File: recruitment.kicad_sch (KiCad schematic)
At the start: 12 parts, among them K1 Relay_SPST-NO, U1 OKI-78SR-5_1.5-W36-C

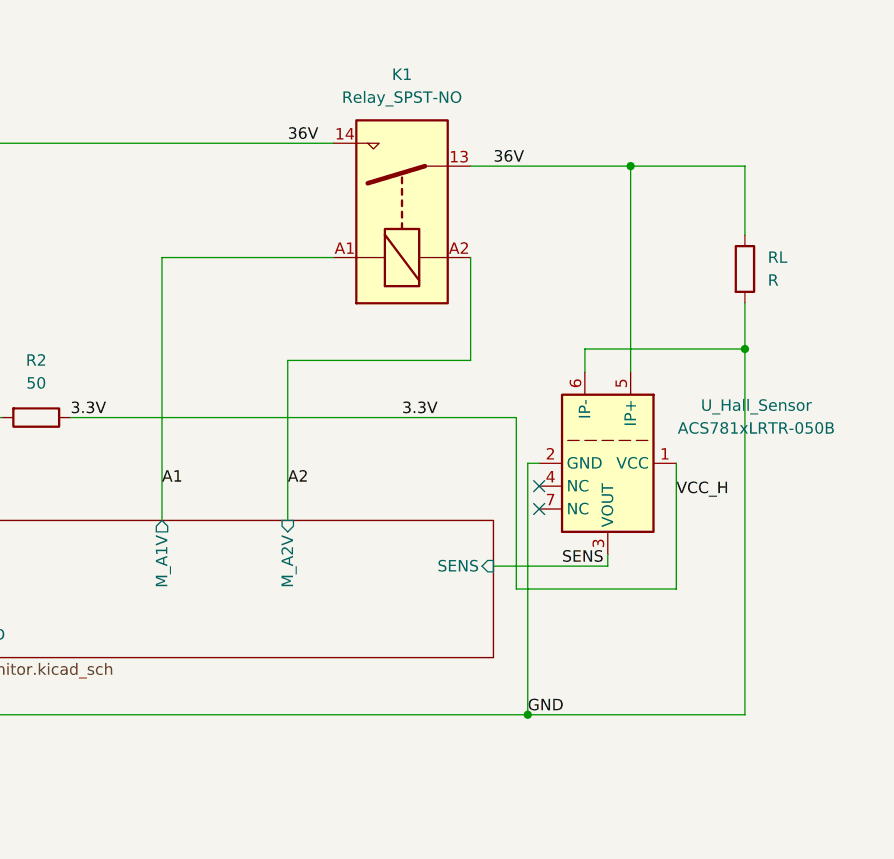
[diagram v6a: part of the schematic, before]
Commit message: comparator wirirng
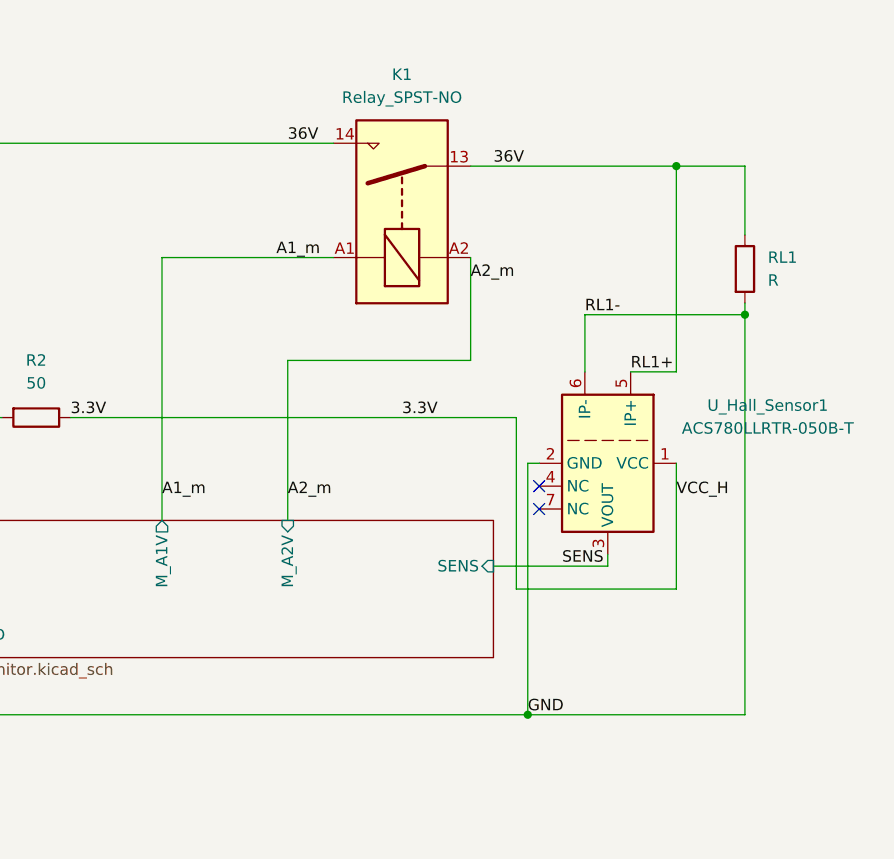
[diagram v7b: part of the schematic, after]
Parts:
- C1: footprint (none) -> Capacitor_SMD:C_0201_0603Metric
- K1: footprint (none) -> LED_THT:LED_D3.0mm
- R1, R2, R3, R4: footprint (none) -> Resistor_SMD:R_0201_0603Metric
- RL1: renamed from RL; footprint (none) -> Resistor_SMD:R_0201_0603Metric
- U_Hall_Sensor1: renamed from U_Hall_Sensor; value ACS781xLRTR-050B -> ACS780LLRTR-050B-T
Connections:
- net A1 renamed A1_m
- net A2 renamed A2_m
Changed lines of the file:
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@@
-	)
-	(junction
-		(at 196.85 41.91)
-		(diameter 0)
-		(color 0 0 0 0)
 	)
 	(junction
@@
 	)
 	(junction
-		(at 209.55 62.23)
-		(diameter 0)
-		(color 0 0 0 0)
-	)
-	(junction
 		(at 115.57 80.01)
 		(diameter 0)
@@
 	)
 	(junction
+		(at 209.55 58.42)
+		(diameter 0)
+		(color 0 0 0 0)
+	)
+	(junction
 		(at 54.61 102.87)
 		(diameter 0)
@@
 	)
 	(junction
+		(at 201.93 41.91)
+		(diameter 0)
+		(color 0 0 0 0)
+	)
+	(junction
 		(at 185.42 102.87)
 		(diameter 0)
@@
 	(wire
 		(pts
-			(xy 196.85 64.77) (xy 196.85 41.91)
-		)
-		(stroke
-			(width 0)
-			(type default)
-		)
-	)
-	(wire
-		(pts
-			(xy 209.55 57.15) (xy 209.55 62.23)
+			(xy 158.75 63.5) (xy 158.75 81.28)
+		)
+		(stroke
+			(width 0)
+			(type default)
+		)
+	)
+	(wire
+		(pts
+			(xy 201.93 64.77) (xy 201.93 41.91)
+		)
+		(stroke
+			(width 0)
+			(type default)
+		)
+	)
+	(wire
+		(pts
+			(xy 209.55 57.15) (xy 209.55 58.42)
 		)
 		(stroke
@@
 	(wire
 		(pts
-			(xy 191.77 62.23) (xy 191.77 64.77)
-		)
-		(stroke
-			(width 0)
-			(type default)
-		)
-	)
-	(wire
-		(pts
 			(xy 46.99 80.01) (xy 67.31 80.01)
 		)
@@
 	(wire
 		(pts
-			(xy 209.55 62.23) (xy 191.77 62.23)
+			(xy 209.55 58.42) (xy 191.77 58.42)
 		)
 		(stroke
@@
 	(wire
 		(pts
-			(xy 209.55 62.23) (xy 209.55 102.87)
+			(xy 209.55 58.42) (xy 209.55 102.87)
 		)
 		(stroke
@@
 	(wire
 		(pts
+			(xy 201.93 41.91) (xy 209.55 41.91)
+		)
+		(stroke
+			(width 0)
+			(type default)
+		)
+	)
+	(wire
+		(pts
 			(xy 74.93 87.63) (xy 74.93 102.87)
 		)
@@
 	(wire
 		(pts
-			(xy 179.07 41.91) (xy 196.85 41.91)
+			(xy 179.07 41.91) (xy 201.93 41.91)
 		)
 		(stroke
@@
 	(wire
 		(pts
-			(xy 158.75 81.28) (xy 158.75 63.5)
+			(xy 191.77 58.42) (xy 191.77 64.77)
 		)
 		(stroke
@@
 	(wire
 		(pts
+			(xy 201.93 64.77) (xy 196.85 64.77)
+		)
+		(stroke
+			(width 0)
+			(type default)
+		)
+	)
+	(wire
+		(pts
 			(xy 185.42 102.87) (xy 209.55 102.87)
 		)
@@
 	(wire
 		(pts
-			(xy 144.78 81.28) (xy 144.78 52.07)
+			(xy 144.78 52.07) (xy 144.78 81.28)
 		)
 		(stroke
@@
 		(pts
 			(xy 181.61 86.36) (xy 194.31 86.36)
-		)
-		(stroke
-			(width 0)
-			(type default)
-		)
-	)
-	(wire
-		(pts
-			(xy 196.85 41.91) (xy 209.55 41.91)
 		)
 		(stroke
@@
 		)
 	)
+	(label "RL1+"
+		(at 196.85 64.77 0)
+		(effects
+			(font
+				(size 1.27 1.27)
+			)
+			(justify left bottom)
+		)
+	)
 	(label "9-17V"
 		(at 60.96 80.01 0)
@@
 		)
 	)
+	(label "A1_m"
+		(at 157.48 52.07 0)
+		(effects
+			(font
+				(size 1.27 1.27)
+			)
+			(justify left bottom)
+		)
+	)
 	(label "3.3V"
 		(at 171.45 69.85 0)
@@
 		)
 	)
+	(label "RL1-"
+		(at 191.77 58.42 0)
+		(effects
+			(font
+				(size 1.27 1.27)
+			)
+			(justify left bottom)
+		)
+	)
 	(label "GND"
 		(at 185.42 102.87 0)
@@
 		)
 	)
-	(label "A1"
-		(at 144.78 77.47 0)
+	(label "A1_m"
+		(at 144.78 78.74 0)
 		(effects
 			(font
@@
 		)
 	)
-	(label "A2"
-		(at 158.75 77.47 0)
+	(label "A2_m"
+		(at 158.75 78.74 0)
+		(effects
+			(font
+				(size 1.27 1.27)
+			)
+			(justify left bottom)
+		)
+	)
+	(label "A2_m"
+		(at 179.07 54.61 0)
 		(effects
 			(font
@@
 		(dnp no)
 		(fields_autoplaced yes)
-		(property "Reference" "U_Hall_Sensor"
-			(at 210.82 68.5098 90)
-			(effects
-				(font
-					(size 1.27 1.27)
-				)
-			)
-		)
-		(property "Value" "ACS781xLRTR-050B"
-			(at 210.82 71.0498 90)
+		(property "Reference" "U_Hall_Sensor1"
+			(at 212.09 68.5098 90)
+			(effects
+				(font
+					(size 1.27 1.27)
+				)
+			)
+		)
+		(property "Value" "ACS780LLRTR-050B-T"
+			(at 212.09 71.0498 90)
 			(effects
 				(font
@@
 			(project ""
 				(path "/bdc7face-9f7c-4701-80bb-4cc144448db1"
-					(reference "U_Hall_Sensor")
+					(reference "U_Hall_Sensor1")
 					(unit 1)
 				)
@@
 			)
 		)
-		(property "Footprint" ""
+		(property "Footprint" "Resistor_SMD:R_0201_0603Metric"
 			(at 119.888 43.18 90)
 			(effects
@@
 			)
 		)
-		(property "Footprint" ""
+		(property "Footprint" "Capacitor_SMD:C_0201_0603Metric"
 			(at 47.9552 97.79 0)
 			(effects
@@
 			)
 		)
-		(property "Footprint" ""
+		(property "Footprint" "Resistor_SMD:R_0201_0603Metric"
 			(at 91.948 87.63 90)
 			(effects
@@
 		(dnp no)
 		(fields_autoplaced yes)
-		(property "Reference" "RL"
+		(property "Reference" "RL1"
 			(at 212.09 52.0699 0)
 			(effects
@@
 			)
 		)
-		(property "Footprint" ""
+		(property "Footprint" "Resistor_SMD:R_0201_0603Metric"
 			(at 207.772 53.34 90)
 			(effects
@@
 			(project ""
 				(path "/bdc7face-9f7c-4701-80bb-4cc144448db1"
-					(reference "RL")
+					(reference "RL1")
 					(unit 1)
 				)
@@
 			)
 		)
-		(property "Footprint" ""
+		(property "Footprint" "Resistor_SMD:R_0201_0603Metric"
 			(at 45.212 87.63 90)
 			(effects
@@
 			)
 		)
-		(property "Footprint" ""
+		(property "Footprint" "LED_THT:LED_D3.0mm"
 			(at 172.72 35.56 0)
 			(effects
@@
 			)
 		)
-		(property "Footprint" ""
+		(property "Footprint" "Resistor_SMD:R_0201_0603Metric"
 			(at 130.81 68.072 90)
 			(effects

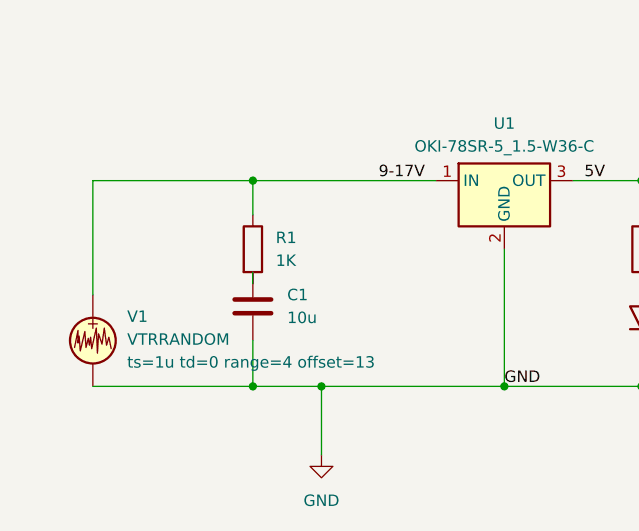
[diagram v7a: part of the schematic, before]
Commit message: added footprints
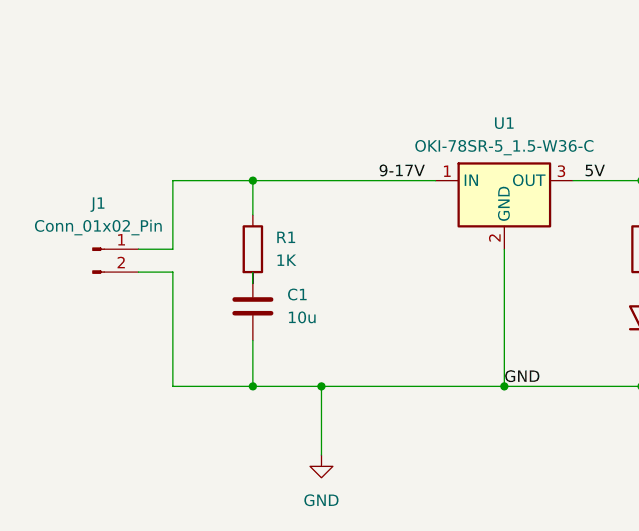
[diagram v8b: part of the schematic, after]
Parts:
- removed V1: VTRRANDOM, symbol Simulation_SPICE:VTRRANDOM
- added J1: Conn_01x02_Pin, Connector_Samtec_MicroPower:Samtec_UMPS-02-XX.X-X-V-S_1x02_P2.0mm_Socket, symbol Connector:Conn_01x02_Pin
- D2, D3: footprint LED_THT:LED_D3.0mm -> LED_THT:LED_D1.8mm_W1.8mm_H2.4mm_Horizontal_O6.35mm_Z4.9mm
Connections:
- net 9-17V: now also J1.1 (Pin_1)
- net GND: now also J1.2 (Pin_2)
